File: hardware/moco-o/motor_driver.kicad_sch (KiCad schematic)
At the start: 66 parts, among them Q3 CSD18540Q5B, Q4 CSD18540Q5B, Q5 CSD18540Q5B, Q6 CSD18540Q5B, Q7 CSD18540Q5B, Q8 CSD18540Q5B, U2 DRV8301

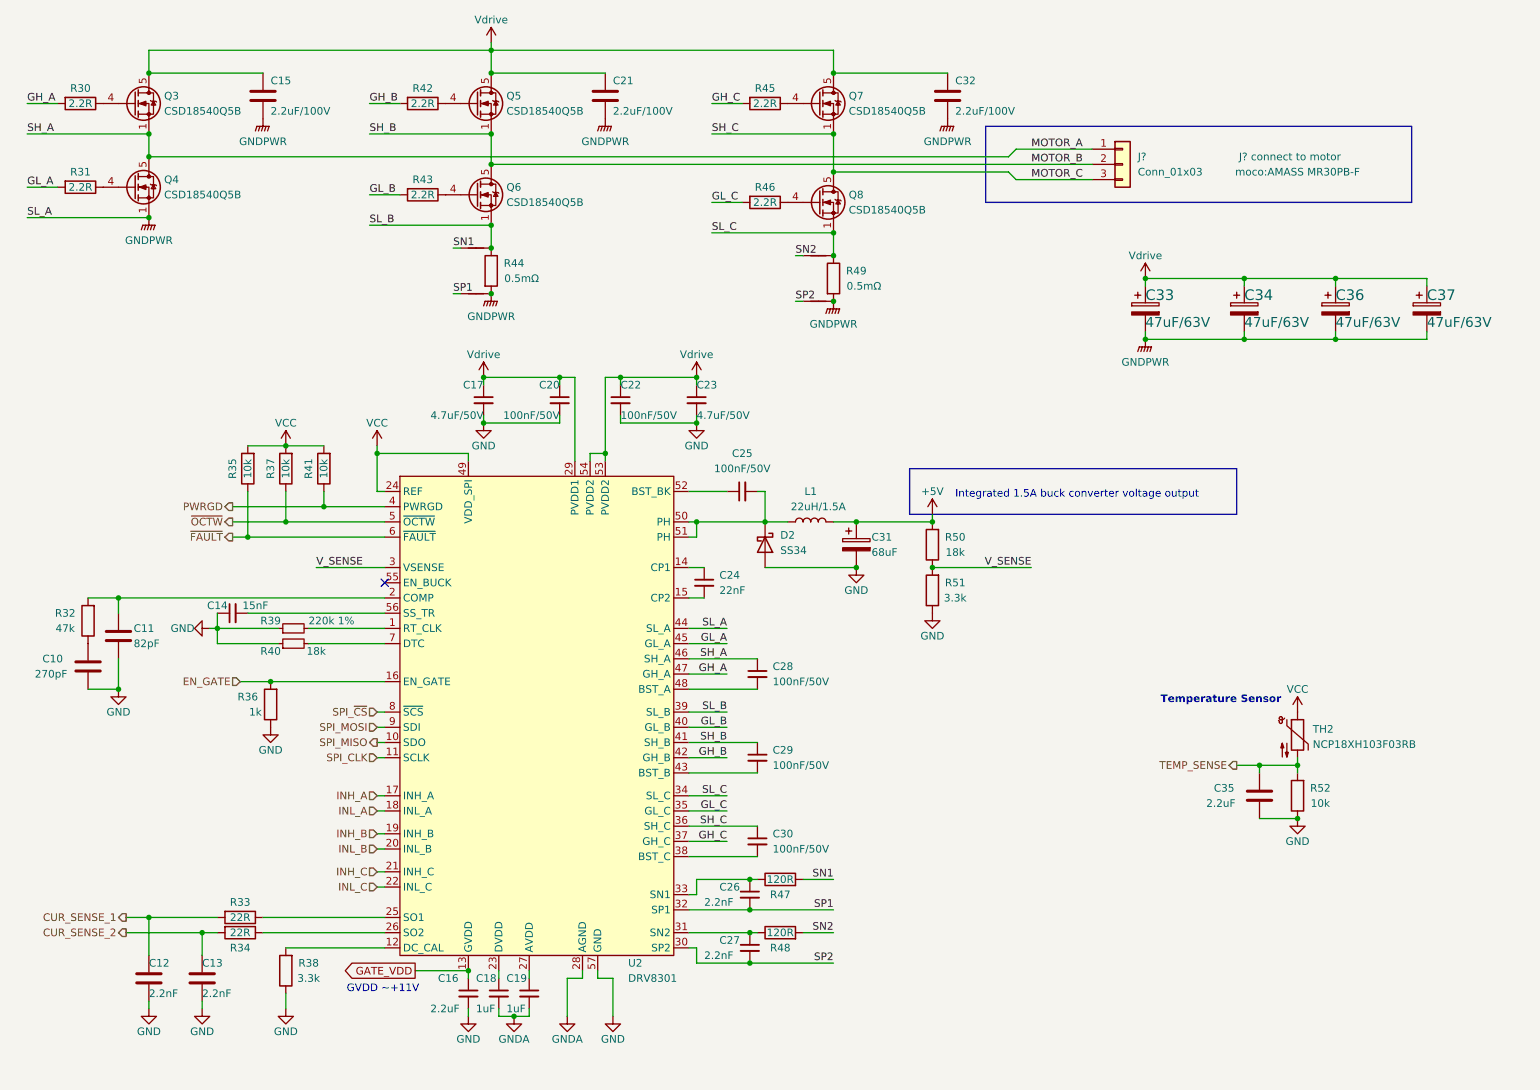
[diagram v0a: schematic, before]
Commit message: Change to DRV8323H
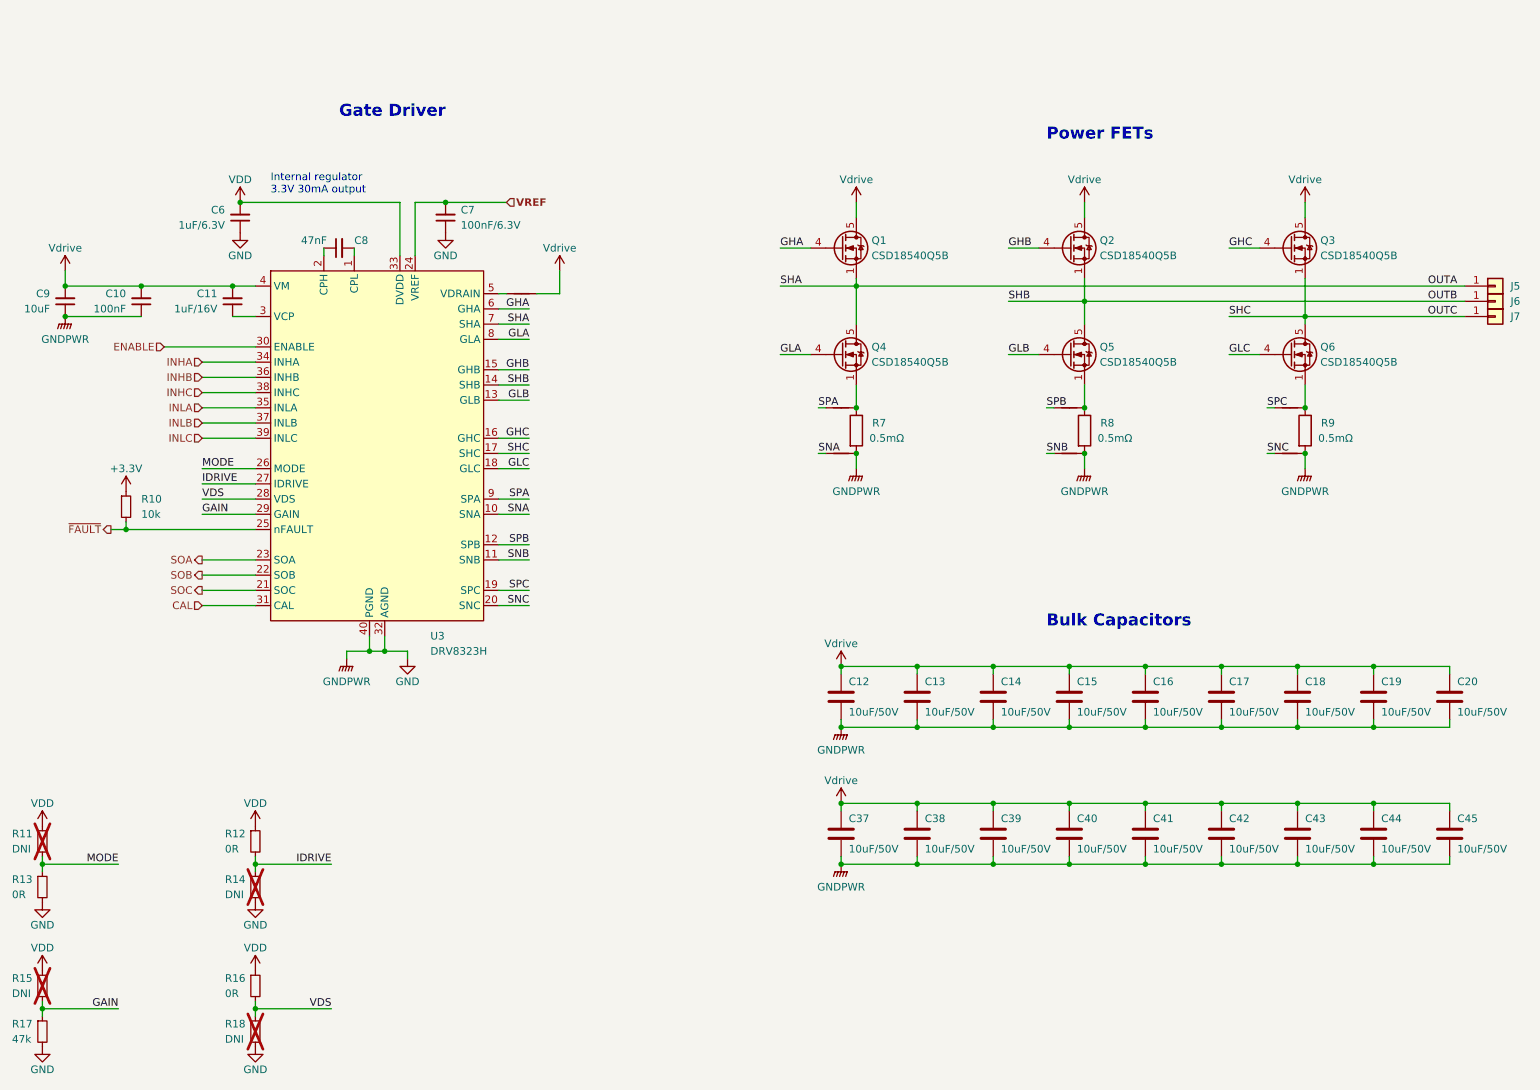
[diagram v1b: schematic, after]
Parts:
- removed C10: 270pF, Capacitor_SMD:C_0402_1005Metric, symbol Device:C
- removed C11: 82pF, Capacitor_SMD:C_0402_1005Metric, symbol Device:C
- removed C14: 15nF, Capacitor_SMD:C_0402_1005Metric, symbol Device:C_Small
- removed C16: 2.2uF, Capacitor_SMD:C_0402_1005Metric, symbol Device:C_Small
- removed C17, C23: 4.7uF/50V, Capacitor_SMD:C_1206_3216Metric, symbol Device:C_Small
- removed C18, C19: 1uF, Capacitor_SMD:C_0402_1005Metric, symbol Device:C_Small
- removed C20, C22, C25, C28, C29, C30: 100nF/50V, Capacitor_SMD:C_0603_1608Metric, symbol Device:C_Small
- removed C21, C32: 2.2uF/100V, Capacitor_SMD:C_1206_3216Metric, symbol Device:C
- removed C24: 22nF, Capacitor_SMD:C_0402_1005Metric, symbol Device:C_Small
- removed C26, C27: 2.2nF, Capacitor_SMD:C_0603_1608Metric, symbol Device:C_Small
- removed C31: 68uF, Capacitor_Tantalum_SMD:CP_EIA-6032-28_Kemet-C, symbol Device:C_Polarized
- removed C33, C34, C36, C37: 47uF/63V, Capacitor_SMD:CP_Elec_8x10, symbol Device:C_Polarized
- removed C35: 2.2uF, Capacitor_SMD:C_0402_1005Metric, symbol Device:C
- removed D2: SS34, Diode_SMD:D_SMA, symbol Diode:MBR340
- removed J?: Conn_01x03, moco:AMASS MR30PB-F, symbol Connector_Generic:Conn_01x03
- removed L1: 22uH/1.5A, Inductor_SMD:L_Bourns-SRN8040_8x8.15mm, symbol Device:L
- removed NT8, NT9: NetTie_2, NetTie:NetTie-2_SMD_Pad0.5mm, symbol Device:NetTie_2
- removed Q7, Q8: CSD18540Q5B, Package_TO_SOT_SMD:TDSON-8-1, symbol Transistor_FET:CSD18540Q5B
- removed R30, R31, R42, R43, R45, R46: 2.2R, Resistor_SMD:R_0603_1608Metric, symbol Device:R
- removed R32: 47k, Resistor_SMD:R_0402_1005Metric, symbol Device:R
- removed R33, R34: 22R, Resistor_SMD:R_0402_1005Metric, symbol Device:R
- removed R35, R37, R41, R52: 10k, Resistor_SMD:R_0402_1005Metric, symbol Device:R
- removed R36: 1k, Resistor_SMD:R_0402_1005Metric, symbol Device:R
- removed R38, R51: 3.3k, Resistor_SMD:R_0402_1005Metric, symbol Device:R
- removed R39: 220k 1%, Resistor_SMD:R_0402_1005Metric, symbol Device:R_Small
- removed R40: 18k, Resistor_SMD:R_0402_1005Metric, symbol Device:R_Small
- removed R44, R49: 0.5mΩ, Resistor_SMD:R_2512_6332Metric, symbol Device:R
- removed R47, R48: 120R, Resistor_SMD:R_0402_1005Metric, symbol Device:R
- removed R50: 18k, Resistor_SMD:R_0402_1005Metric, symbol Device:R
- removed TH2: NCP18XH103F03RB, Resistor_SMD:R_0603_1608Metric, symbol Device:Thermistor_NTC
- removed U2: DRV8301, Package_SO:HTSSOP-56-1EP_6.1x14mm_P0.5mm_EP3.61x6.35mm, symbol moco:DRV8301
- added C10: 100nF, Capacitor_SMD:C_0402_1005Metric, symbol Device:C_Small
- added C11: 1uF/16V, Capacitor_SMD:C_0603_1608Metric, symbol Device:C_Small
- added C14, C16, C17, C18, C19, C20: 10uF/50V, Capacitor_SMD:C_1206_3216Metric, symbol Device:C
- added C37, C38, C39, C40, C41, C42, C43, C44, C45: 10uF/50V, Capacitor_SMD:C_1206_3216Metric_Pad1.33x1.80mm_HandSolder, symbol Device:C
- added C6: 1uF/6.3V, Capacitor_SMD:C_0402_1005Metric, symbol Device:C_Small
- added C7: 100nF/6.3V, Capacitor_SMD:C_0402_1005Metric, symbol Device:C_Small
- added C8: 47nF, Capacitor_SMD:C_0603_1608Metric, symbol Device:C_Small
- added C9: 10uF, Capacitor_SMD:C_0603_1608Metric, symbol Device:C_Small
- added J5: A, moco:wire_3.2mm, symbol Connector_Generic:Conn_01x01
- added J6: B, moco:wire_3.2mm, symbol Connector_Generic:Conn_01x01
- added J7: C, moco:wire_3.2mm, symbol Connector_Generic:Conn_01x01
- added NT1, NT2, NT3, NT4, NT7: NetTie_2, NetTie:NetTie-2_SMD_Pad0.5mm, symbol Device:NetTie_2
- added Q1, Q2: CSD18540Q5B, Package_TO_SOT_SMD:TDSON-8-1, symbol Transistor_FET:CSD18540Q5B
- added R10: 10k, Resistor_SMD:R_0402_1005Metric, symbol Device:R_Small
- added R11, R14, R15, R18: DNI, Resistor_SMD:R_0402_1005Metric_Pad0.72x0.64mm_HandSolder, symbol Device:R_Small
- added R12, R13, R16: 0R, Resistor_SMD:R_0402_1005Metric_Pad0.72x0.64mm_HandSolder, symbol Device:R_Small
- added R17: 47k, Resistor_SMD:R_0402_1005Metric_Pad0.72x0.64mm_HandSolder, symbol Device:R_Small
- added R7, R8, R9: 0.5mΩ, Resistor_SMD:R_2512_6332Metric, symbol Device:R
- added U3: DRV8323H, Package_DFN_QFN:QFN-40-1EP_6x6mm_P0.5mm_EP4.6x4.6mm_ThermalVias, symbol moco:DRV8323H
- C12, C13: value 2.2nF -> 10uF/50V; footprint Capacitor_SMD:C_0603_1608Metric -> Capacitor_SMD:C_1206_3216Metric; JLCPCB Part # C1604 -> C2991915; MFR.Part # 0603B222K500NT -> C1206B106K050TEF
- C15: value 2.2uF/100V -> 10uF/50V; JLCPCB Part # C650969 -> C2991915; MFR.Part # HMK316AC7225KLHTE -> C1206B106K050TEF
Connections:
- net CUR_SENSE_1 is gone; now on net Vdrive: C12.1
- net CUR_SENSE_2 is gone; now on net Vdrive: C13.1
- net GND: now also C15.2, NT5.2, NT6.2, C10.1, C14.2, C16.2, C17.2, C18.2, C19.2, C20.2, C37.2, C38.2, C39.2, C40.2, C41.2, C42.2, C43.2, C44.2, C45.2, C6.1, C7.1, C9.1, NT4.2, R13.2, R14.2, R17.2, R18.2, R7.2, R8.2, R9.2, U3.32 (AGND), U3.40 (PGND), U3.41 (GND)
- net Vdrive: now also C10.2, C11.2, C14.1, C16.1, C17.1, C18.1, C19.1, C20.1, C37.1, C38.1, C39.1, C40.1, C41.1, C42.1, C43.1, C44.1, C45.1, C9.2, NT7.1, Q1.5 (D), Q2.5 (D), U3.4 (VM); no longer Q5.5 (D)
- net ~{FAULT}: now also R10.2, U3.25 (nFAULT)
- net GLC: now reaches Q6.4 (G)
- net GLC: now also U3.18 (GLC)
- net GLB: now reaches Q5.4 (G)
- net GLB: now also U3.13 (GLB)
- net GLA: now reaches Q4.4 (G)
- net GLA: now also U3.8 (GLA)
- net GHC: now reaches Q3.4 (G)
- net GHC: now also U3.16 (GHC)
- net GNDPWR: no longer names the net of Q4.1 (S), Q4.2 (S), Q4.3 (S)
- net GNDPWR: now also NT1.2, R7.1; no longer C15.2, NT6.2
- net MOTOR_A renamed OUTC
- net OUTC: now also Q6.5 (D), J7.1 (Pin_1), U3.17 (SHC); no longer Q4.5 (D)
- net MOTOR_B: no longer names the net of Q5.1 (S), Q5.2 (S), Q5.3 (S)
- net MOTOR_B: now also NT2.2, R8.1; no longer Q6.5 (D)
- net SL_B: no longer names the net of Q6.1 (S), Q6.2 (S), Q6.3 (S)
- net SL_B: now also NT3.2, R9.1; no longer NT5.2
- net SN1 renamed SNB
- net SNB: now also U3.11 (SNB)
- net SP1 renamed SNC
- net SNC: now also U3.20 (SNC)
- new net: C8.2, U3.1 (CPL)
- new net: C8.1, U3.2 (CPH)
- new net: C11.1, U3.3 (VCP)
- new net: NT7.2, U3.5 (VDRAIN)
- new net +3.3V: R10.1
- new net CAL: U3.31 (CAL)
- new net ENABLE: U3.30 (ENABLE)
- new net GAIN: R15.2, R17.1, U3.29 (GAIN)
- new net GHA: Q1.4 (G), U3.6 (GHA)
- new net GHB: Q2.4 (G), U3.15 (GHB)
- new net IDRIVE: R12.2, R14.1, U3.27 (IDRIVE)
- new net INHA: U3.34 (INHA)
- new net INHB: U3.36 (INHB)
- new net INHC: U3.38 (INHC)
- new net INLA: U3.35 (INLA)
- new net INLB: U3.37 (INLB)
- new net INLC: U3.39 (INLC)
- new net MODE: R11.2, R13.1, U3.26 (MODE)
- new net OUTA: J5.1 (Pin_1), Q1.1 (S), Q1.2 (S), Q1.3 (S), Q4.5 (D), U3.7 (SHA)
- new net OUTB: J6.1 (Pin_1), Q2.1 (S), Q2.2 (S), Q2.3 (S), Q5.5 (D), U3.14 (SHB)
- new net SNA: NT4.1, U3.10 (SNA)
- new net SOA: U3.23 (SOA)
- new net SOB: U3.22 (SOB)
- new net SOC: U3.21 (SOC)
- new net SPA: NT1.1, U3.9 (SPA)
- new net SPB: NT2.1, U3.12 (SPB)
- new net SPC: NT3.1, U3.19 (SPC)
- new net VDD: C6.2, R11.1, R12.1, R15.1, R16.1, U3.33 (DVDD)
- new net VDS: R16.2, R18.1, U3.28 (VDS)
- new net VREF: C7.2, U3.24 (VREF)
- no-connect marks 1 -> 0
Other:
- note added: "Bulk Capacitors"
- note added: "Gate Driver"
- note added: "Internal regulator 3.3V 30mA output"
- note added: "Power FETs"
- note removed: "GVDD ~+11V"
- note removed: "Integrated 1.5A buck converter voltage output"
- note removed: "Temperature Sensor"
